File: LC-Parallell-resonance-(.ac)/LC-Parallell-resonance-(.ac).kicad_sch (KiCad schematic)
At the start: 4 parts

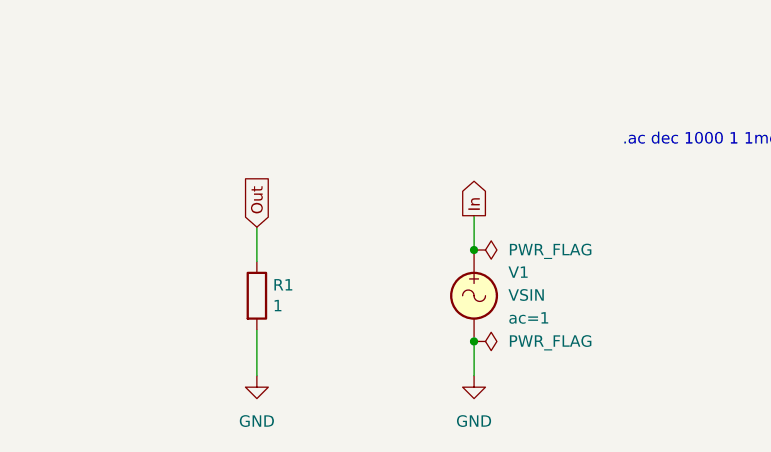
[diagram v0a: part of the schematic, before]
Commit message: Updated all schematics and prepared for KiCad 8.0
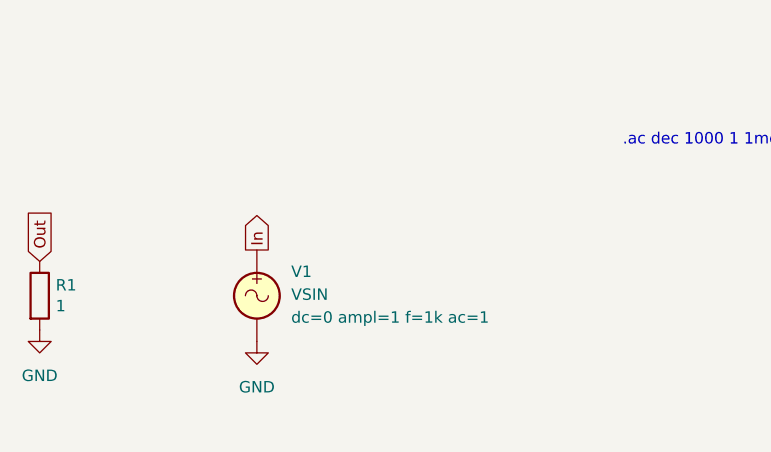
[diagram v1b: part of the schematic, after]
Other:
- moved on the sheet: R1
